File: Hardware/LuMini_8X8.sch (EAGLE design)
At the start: 74 parts, among them J1 LED_PADCIRCULARPAD, J2 LED_PADCIRCULARPAD, J3 LED_PADCIRCULARPAD, J4 LED_PADCIRCULARPAD, J5 LED_PADCIRCULARPAD, J6 LED_PADCIRCULARPAD, J7 LED_PADCIRCULARPAD, J8 LED_PADCIRCULARPAD

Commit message: pre design review
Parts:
- added C1: DNP, SparkFun-Capacitors:4.7UF-1206-16V-(+80/-20%)
- added H1, H2, H3, H4: STANDOFF_ELECTRICALSTANDOFF-ELECTRICAL-NOTHERMALS, SparkFun-Hardware:STANDOFF_ELECTRICALSTANDOFF-ELECTRICAL-NOTHERMALS
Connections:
- net 5V: now also C1.1
- net GND: now also C1.2, H1.P$1, H2.P$1, H3.P$1, H4.P$1
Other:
- note added: "Andy England"
- note added: "Heat Sinking Standoffs"
- note added: "LED's"
- note added: "v02"
- moved on the sheet: D1, D10, D11, D12, D13, D14, D15, D16, D17, D18, D19, D2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

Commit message: updating to 4 layer
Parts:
- added FD1, FD2, FD3, FD4: FIDUCIALUFIDUCIAL, SparkFun-Aesthetics:FIDUCIALUFIDUCIAL
- added J10, J11, J12, J13, J14, J15, J16, J9: LED_PAD, SparkFun-Connectors:LED_PAD
- added LOGO2: OSHW-LOGOS, SparkFun-Aesthetics:OSHW-LOGOS
- H1, H2, H3, H4: value STANDOFF_ELECTRICALSTANDOFF-ELECTRICAL-NOTHERMALS -> STANDOFF_ELECTRICAL-NOTHERMALS; device SparkFun-Hardware:STANDOFF_ELECTRICALSTANDOFF-ELECTRICAL-NOTHERMALS -> SparkFun-Hardware:STANDOFF_ELECTRICAL-NOTHERMALS
- J1, J2, J3, J4, J5, J6, J7, J8: value LED_PADCIRCULARPAD -> LED_PAD; device Andy:LED_PADCIRCULARPAD -> SparkFun-Connectors:LED_PAD
- LOGO1: value SFE_LOGO_NAME_FLAME.2_INCH -> SFE_LOGO_NAME_FLAME.1_INCH; device SparkFun-Aesthetics:SFE_LOGO_NAME_FLAME.2_INCH -> SparkFun-Aesthetics:SFE_LOGO_NAME_FLAME.1_INCH
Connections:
- net 5V: now also H1.P$1, H2.P$1, H3.P$1, H4.P$1, J1.1, J2.1
- net CI: now also J10.1, J9.1; no longer J4.1
- net CO: now also J13.1, J14.1; no longer J1.1
- net DI: now also J11.1, J12.1; no longer J3.1
- net DO: now also J15.1, J16.1; no longer J2.1
- net GND: now also J3.1, J4.1; no longer H1.P$1, H2.P$1, H3.P$1, H4.P$1
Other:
- note added: "Decoupling Capacitor"
- note added: "LED Connection Pads"
- note added: "Vin: 3.0V-5.5V"
- moved on the sheet: C1, J1, J2, J3, J4, J5, J6, J7, J8

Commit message: changing heatsinks back to ground
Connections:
- net 5V: no longer H1.P$1, H2.P$1, H3.P$1, H4.P$1
- net GND: now also H1.P$1, H2.P$1, H3.P$1, H4.P$1
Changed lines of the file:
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@@
 <part name="J15" library="SparkFun-Connectors" deviceset="LED_PAD" device=""/>
 <part name="J16" library="SparkFun-Connectors" deviceset="LED_PAD" device=""/>
-<part name="SUPPLY67" library="SparkFun-PowerSymbols" deviceset="5V" device=""/>
 <part name="LOGO2" library="SparkFun-Aesthetics" deviceset="OSHW-LOGO" device="S"/>
 <part name="FD1" library="SparkFun-Aesthetics" deviceset="FIDUCIAL" device="UFIDUCIAL"/>
@@
 <part name="FD3" library="SparkFun-Aesthetics" deviceset="FIDUCIAL" device="UFIDUCIAL"/>
 <part name="FD4" library="SparkFun-Aesthetics" deviceset="FIDUCIAL" device="UFIDUCIAL"/>
+<part name="GND66" library="SparkFun-PowerSymbols" deviceset="GND" device=""/>
 </parts>
 <sheets>
@@
 <instance part="J15" gate="G$1" x="132.08" y="35.56" rot="R180"/>
 <instance part="J16" gate="G$1" x="132.08" y="25.4" rot="R180"/>
-<instance part="SUPPLY67" gate="G$1" x="226.06" y="63.5"/>
 <instance part="LOGO2" gate="G$1" x="408.94" y="48.26"/>
 <instance part="FD1" gate="G$1" x="408.94" y="20.32"/>
@@
 <instance part="FD3" gate="G$1" x="414.02" y="20.32"/>
 <instance part="FD4" gate="G$1" x="416.56" y="20.32"/>
+<instance part="GND66" gate="1" x="226.06" y="5.08"/>
 </instances>
 <busses>
@@
 <wire x1="292.1" y1="33.02" x2="292.1" y2="35.56" width="0.1524" layer="91"/>
 </segment>
+<segment>
+<pinref part="H4" gate="G$1" pin="P$1"/>
+<wire x1="223.52" y1="60.96" x2="226.06" y2="60.96" width="0.1524" layer="91"/>
+<wire x1="226.06" y1="60.96" x2="226.06" y2="45.72" width="0.1524" layer="91"/>
+<pinref part="H3" gate="G$1" pin="P$1"/>
+<wire x1="226.06" y1="45.72" x2="226.06" y2="30.48" width="0.1524" layer="91"/>
+<wire x1="226.06" y1="30.48" x2="226.06" y2="15.24" width="0.1524" layer="91"/>
+<wire x1="223.52" y1="15.24" x2="226.06" y2="15.24" width="0.1524" layer="91"/>
+<pinref part="H2" gate="G$1" pin="P$1"/>
+<wire x1="223.52" y1="30.48" x2="226.06" y2="30.48" width="0.1524" layer="91"/>
+<junction x="226.06" y="30.48"/>
+<pinref part="H1" gate="G$1" pin="P$1"/>
+<wire x1="223.52" y1="45.72" x2="226.06" y2="45.72" width="0.1524" layer="91"/>
+<junction x="226.06" y="45.72"/>
+<pinref part="GND66" gate="1" pin="GND"/>
+<wire x1="226.06" y1="15.24" x2="226.06" y2="7.62" width="0.1524" layer="91"/>
+<junction x="226.06" y="15.24"/>
+</segment>
 </net>
 <net name="5V" class="0">
@@
 <wire x1="292.1" y1="45.72" x2="292.1" y2="43.18" width="0.1524" layer="91"/>
 </segment>
-<segment>
-<pinref part="H4" gate="G$1" pin="P$1"/>
-<wire x1="223.52" y1="60.96" x2="226.06" y2="60.96" width="0.1524" layer="91"/>
-<wire x1="226.06" y1="60.96" x2="226.06" y2="45.72" width="0.1524" layer="91"/>
-<pinref part="H3" gate="G$1" pin="P$1"/>
-<wire x1="226.06" y1="45.72" x2="226.06" y2="30.48" width="0.1524" layer="91"/>
-<wire x1="226.06" y1="30.48" x2="226.06" y2="15.24" width="0.1524" layer="91"/>
-<wire x1="223.52" y1="15.24" x2="226.06" y2="15.24" width="0.1524" layer="91"/>
-<pinref part="H2" gate="G$1" pin="P$1"/>
-<wire x1="223.52" y1="30.48" x2="226.06" y2="30.48" width="0.1524" layer="91"/>
-<junction x="226.06" y="30.48"/>
-<pinref part="H1" gate="G$1" pin="P$1"/>
-<wire x1="223.52" y1="45.72" x2="226.06" y2="45.72" width="0.1524" layer="91"/>
-<junction x="226.06" y="45.72"/>
-<pinref part="SUPPLY67" gate="G$1" pin="5V"/>
-<wire x1="226.06" y1="63.5" x2="226.06" y2="60.96" width="0.1524" layer="91"/>
-<junction x="226.06" y="60.96"/>
-</segment>
 </net>

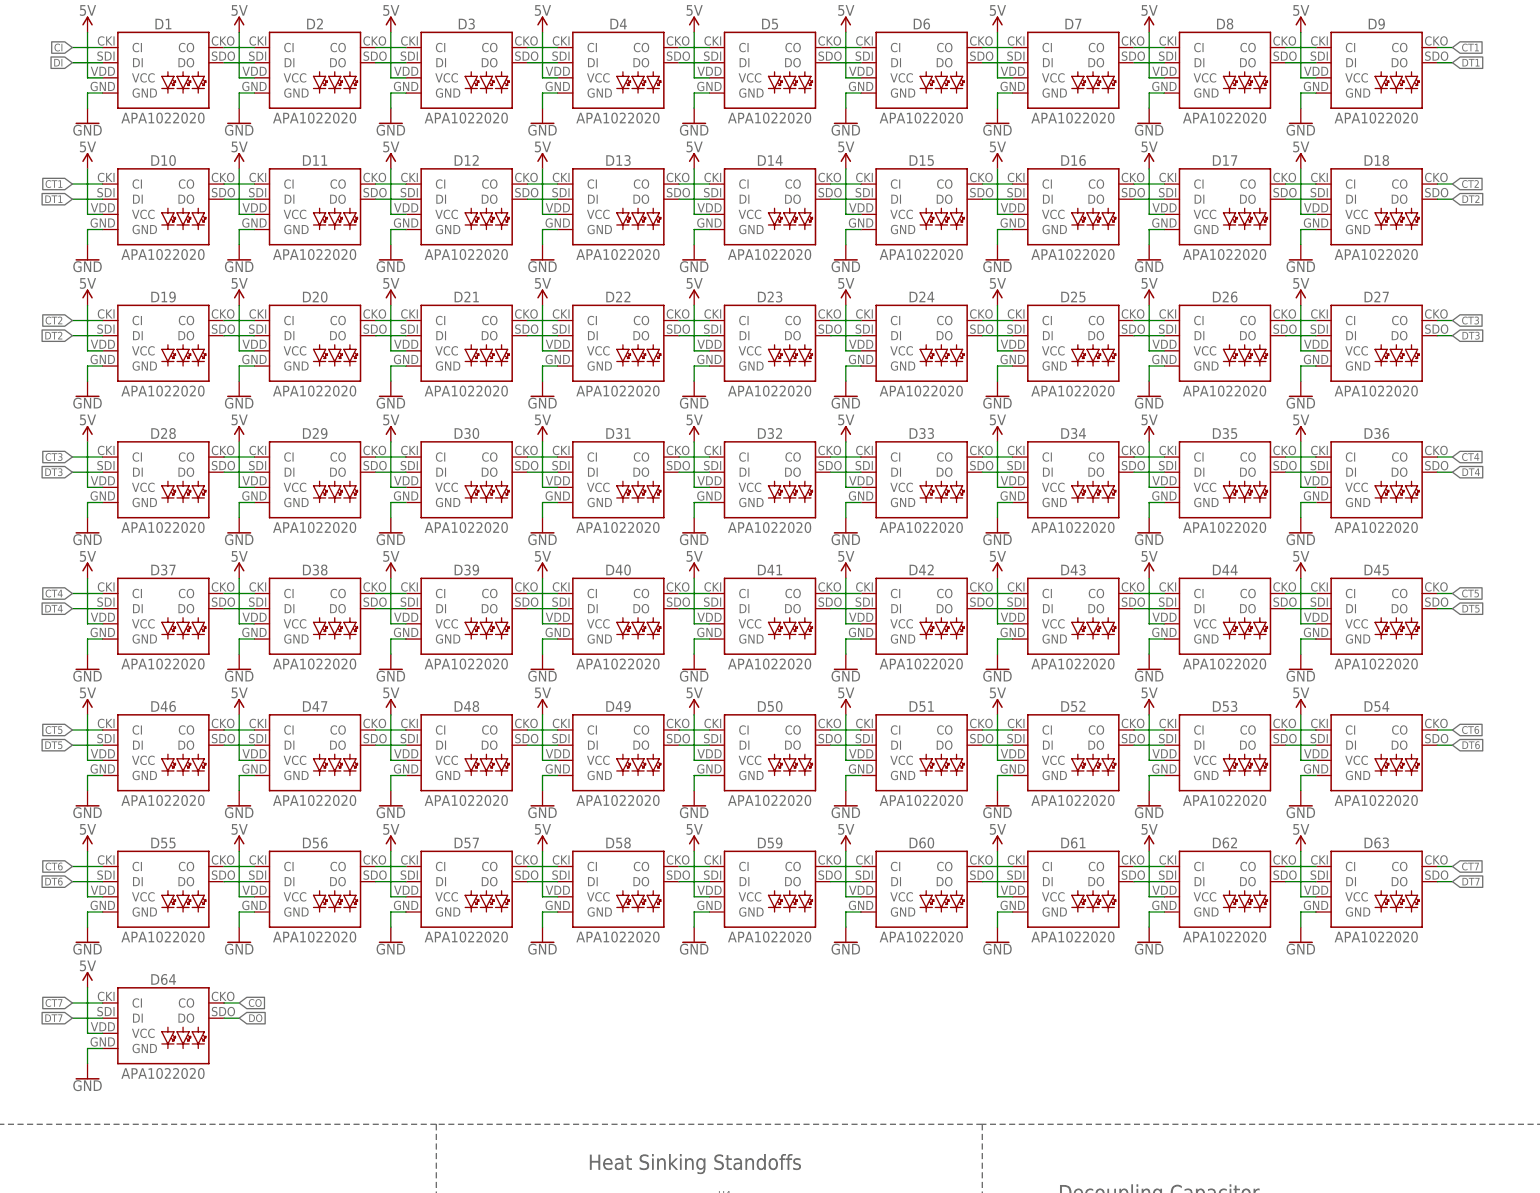
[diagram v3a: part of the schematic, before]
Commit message: updating to proper footprint
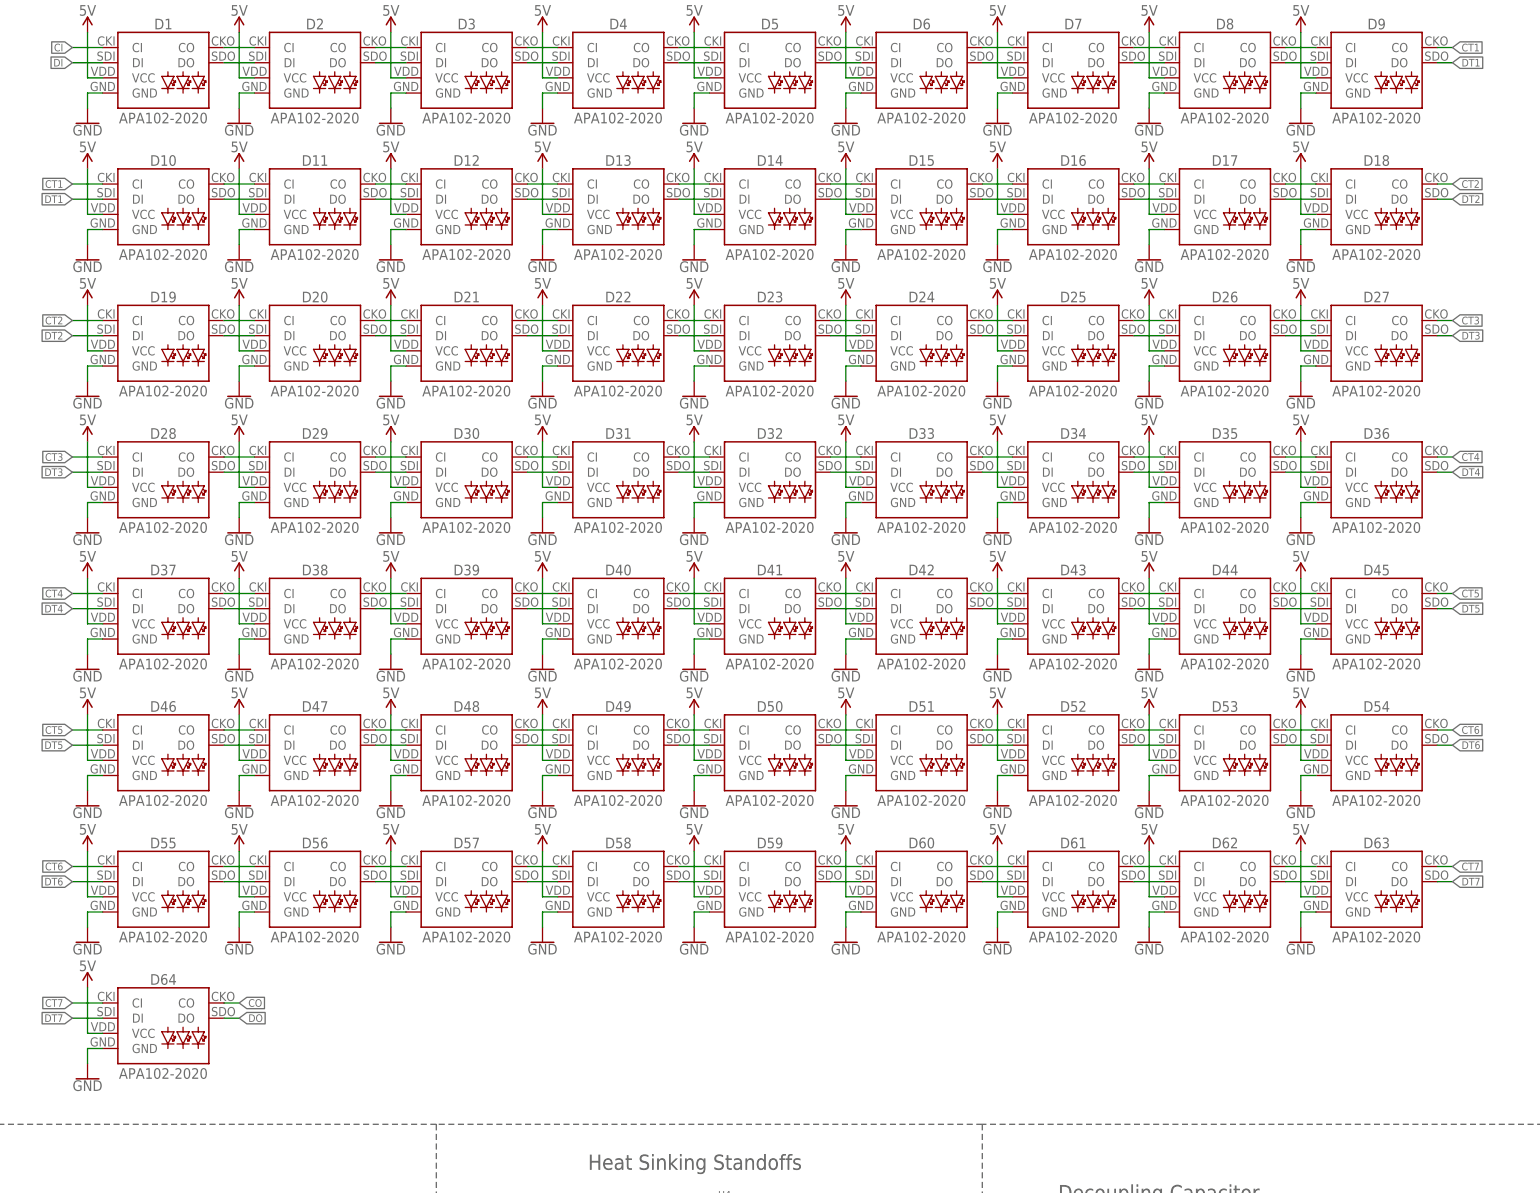
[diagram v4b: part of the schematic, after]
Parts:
- D1, D10, D11, D12, D13, D14, D15, D16, D17, D18, D19, D2, D20, D21, D22, D23, D24, D25, D26, D27, D28, D29, D3, D30, D31, D32, D33, D34, D35, D36, D37, D38, D39, D4, D40, D41, D42, D43, D44, D45, D46, D47, D48, D49, D5, D50, D51, D52, D53, D54, D55, D56, D57, D58, D59, D6, D60, D61, D62, D63, D64, D7, D8, D9: value APA1022020 -> APA102-2020; device SparkFun-LED:APA1022020 -> SparkFun-LED:APA102-2020

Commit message: updating copper to v10
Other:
- note added: "v10"
- note removed: "v02"
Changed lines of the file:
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@@
 <text x="193.04" y="71.12" size="2.54" layer="97" font="vector">Heat Sinking Standoffs</text>
 <text x="348.488" y="11.43" size="2.54" layer="94" font="vector">Andy England</text>
-<text x="419.1" y="7.112" size="2.54" layer="94" font="vector">v02</text>
+<text x="419.1" y="7.112" size="2.54" layer="94" font="vector">v10</text>
 <text x="58.42" y="71.12" size="2.54" layer="97" font="vector">LED Connection Pads</text>
 <text x="271.78" y="66.04" size="2.54" layer="97" font="vector">Decoupling Capacitor</text>
